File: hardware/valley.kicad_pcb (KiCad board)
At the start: 2 copper layers, 28 parts, among them IC1 ATMEGA1284P-A, P1 CONN_01X10, P2 USB_OTG, P3 CONN_02X03, P4 CONN_01X16, Q2 BSS138, U1 CH340G, U2 AP111733, U3 TXS0108E, Y1 12M

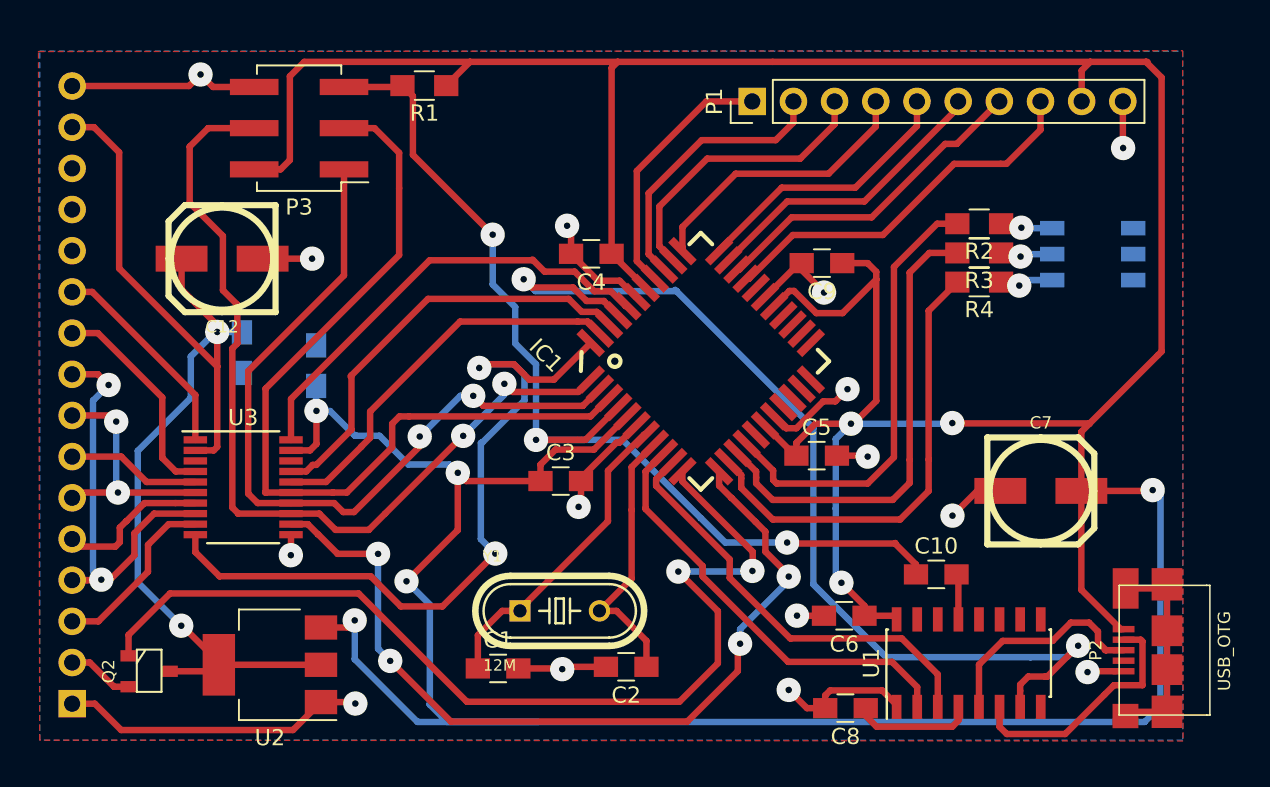
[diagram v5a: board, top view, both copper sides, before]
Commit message: ESP12E version laid out.
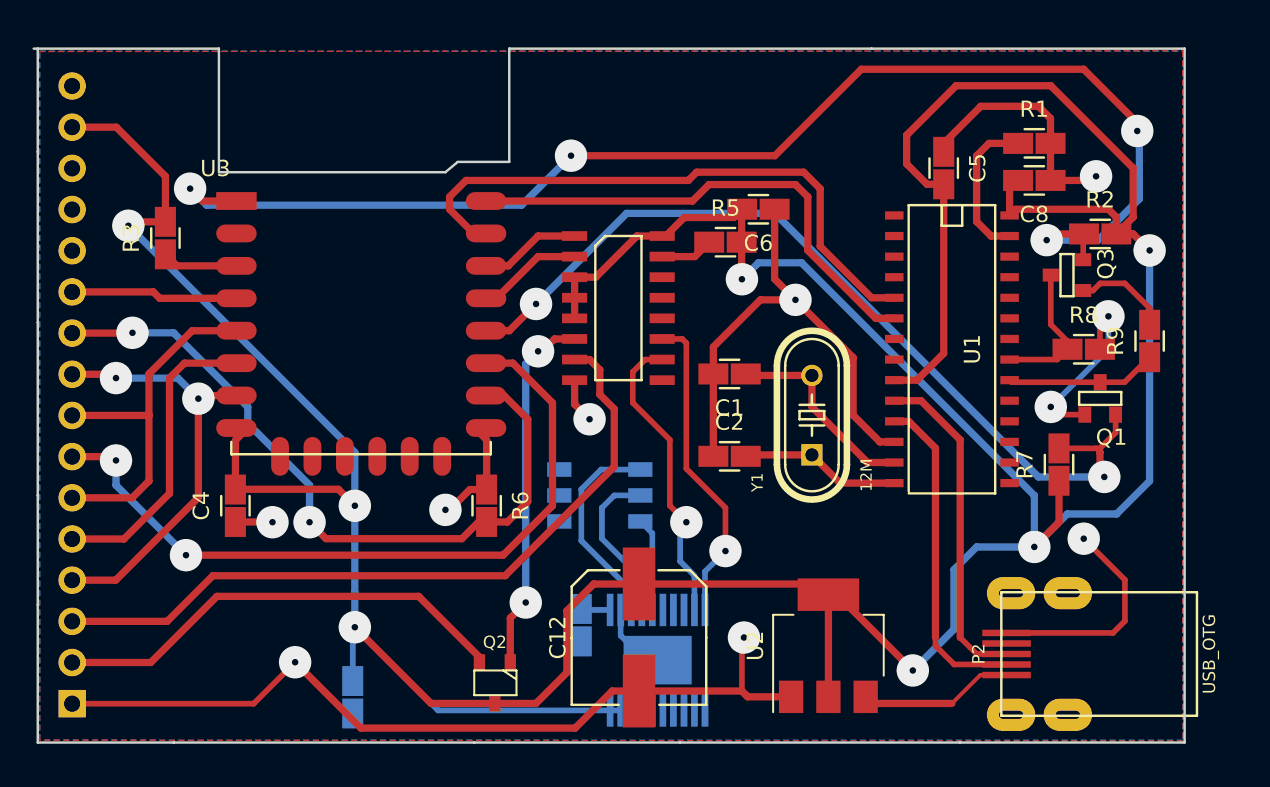
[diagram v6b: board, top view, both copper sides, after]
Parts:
- removed C10, C11, C13, C9: 0.1u, Capacitors_SMD:C_0805_HandSoldering
- removed C7: 47u, cbrues/kicad-lib2/footprints/capacitors.pretty:SMD_PANASONIC_D
- removed P1: CONN_01X10, Pin_Headers:Pin_Header_Straight_1x10_Pitch2.54mm
- removed P3: CONN_02X03, Pin_Headers:Pin_Header_Straight_2x03_Pitch2.54mm_SMD
- added ??1: PCA9557, adamgreig/agg-kicad/agg.pretty:SOIC-16, F.Cu at (155.2, 53.8)
- added Q1: PDTD113ZT,215, celeritous/KiCad.pretty:SOT23-3, F.Cu at (184.9, 58.4)
- added Q3: PDTD113ZT,215, celeritous/KiCad.pretty:SOT23-3, F.Cu at (181.9, 51.8)
- added R5: 2k, coddingtonbear/coddingtonbear.pretty:0805_Milling, F.Cu at (161.8, 49.8)
- added R6: 100k, coddingtonbear/coddingtonbear.pretty:0805_Milling, F.Cu at (147.1, 66.0)
- added R7: 4.7k, coddingtonbear/coddingtonbear.pretty:0805_Milling, F.Cu at (182.4, 63.5)
- added R8: 10k, coddingtonbear/coddingtonbear.pretty:0805_Milling, F.Cu at (183.9, 56.4)
- added R9: 10k, coddingtonbear/coddingtonbear.pretty:0805_Milling, F.Cu at (188.0, 55.9)
- C1, C2, C4, C5, C6, C8: footprint Capacitors_SMD:C_0805_HandSoldering -> coddingtonbear/coddingtonbear.pretty:0805_Milling
- C12: value 47u -> 1000u; footprint cbrues/kicad-lib2/footprints/capacitors.pretty:SMD_PANASONIC_D -> ohdsp/KiCad-Libs/MyKiCadLibs-Footprints.pretty:CAP-SMD-SIZE-F
- C3: footprint Capacitors_SMD:C_0805_HandSoldering -> coddingtonbear/coddingtonbear.pretty:0805_Milling; moved to B.Cu
- IC1: value ATMEGA1284P-A -> TLC5971_SOP; footprint OLIMEX/KiCAD/KiCAD_Footprints/OLIMEX_IC-FP.pretty:TQFP44 -> brunoeagle/kicad-open-modules:TSSOP-20; moved to B.Cu
- P2: footprint valley:MICRO-B_USB-INVERTED -> coddingtonbear/coddingtonbear.pretty:UJ2-MIBH-4-SMT
- R1: value 10k -> R; footprint Resistors_SMD:R_0805_HandSoldering -> coddingtonbear/coddingtonbear.pretty:0805_Milling
- R2, R3: value 1.5k -> 10k; footprint Resistors_SMD:R_0805_HandSoldering -> coddingtonbear/coddingtonbear.pretty:0805_Milling
- R4: value 1k -> 5k; footprint Resistors_SMD:R_0805_HandSoldering -> coddingtonbear/coddingtonbear.pretty:0805_Milling; moved to B.Cu
- U1: value CH340G -> CH341A; footprint Housings_SOIC:SOIC-16_3.9x9.9mm_Pitch1.27mm -> KiCad/SMD_Packages.pretty:SOIC-28
- U3: value TXS0108E -> ESP-12E; footprint Housings_SSOP:TSSOP-20_4.4x6.5mm_Pitch0.65mm -> coddingtonbear/coddingtonbear.pretty:ESP-12E
- moved R3 50.2 mm to (127.3, 49.5), turned to 90 degrees
- moved R1 37.8 mm to (180.8, 43.7), turned to 0 degrees
- moved C12 34.7 mm to (156.5, 74.2), turned to 0 degrees
- moved C8 34.6 mm to (180.8, 46.0)
- moved U2 34.5 mm to (168.1, 74.7), turned to 90 degrees
- moved D1 33.8 mm to (154.1, 65.4), turned to 0 degrees
- moved R4 32.4 mm to (152.9, 73.4), turned to 270 degrees
- moved C4 26.9 mm to (131.6, 66.0), turned to 90 degrees
- moved C6 25.6 mm to (163.8, 47.8)
- moved C1 23.1 mm to (162.1, 57.9), turned to 180 degrees
- moved Q2 21.3 mm to (147.6, 77.0), turned to 180 degrees
- moved Y1 19.7 mm to (167.1, 60.5), turned to 90 degrees
- moved C5 19.4 mm to (175.3, 45.2), turned to 270 degrees
- moved U1 19.4 mm to (175.8, 56.4), turned to 270 degrees
- moved IC1 18.6 mm to (157.6, 75.6), turned to 0 degrees
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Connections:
- C2 pad 1: Net-(C2-Pad1) -> GND
- C2 pad 2: GND -> Net-(C2-Pad2)
- C3 pad 1: +5V -> GND
- C3 pad 2: GND -> +3V3
- C4 pad 1: +5V -> GND
- C4 pad 2: GND -> +3V3
- C5 pad 1: +5V -> GND
- C5 pad 2: GND -> +3V3
- C6 pad 1: +5V -> GND
- C6 pad 2: GND -> +3V3
- C8 pad 1: Net-(C8-Pad1) -> GND
- C8 pad 2: GND -> +3V3
- D1 pad 4: Net-(D1-Pad4) -> LED_BLUE
- D1 pad 5: Net-(D1-Pad5) -> LED_GREEN
- D1 pad 6: Net-(D1-Pad6) -> LED_RED
- IC1 pad 1: MOSI -> Net-(IC1-Pad1)
- IC1 pad 10: TXD -> Net-(??1-Pad11)
- IC1 pad 11: BACKLIGHT -> Net-(IC1-Pad11)
- IC1 pad 12: CS_SD -> Net-(IC1-Pad12)
- IC1 pad 13: LED_RED -> Net-(IC1-Pad13)
- IC1 pad 14: LED_GREEN -> Net-(IC1-Pad14)
- IC1 pad 15: LED_BLUE -> Net-(IC1-Pad15)
- IC1 pad 17: +5V -> Net-(IC1-Pad17)
- IC1 pad 18: GND -> Net-(IC1-Pad18)
- IC1 pad 19: Net-(IC1-Pad19) -> +3V3
- IC1 pad 2: MISO -> GND
- IC1 pad 20: Net-(IC1-Pad20) -> +3V3
- IC1 pad 21: Net-(IC1-Pad21) -> GND
- IC1 pad 3: SCK -> LED_RED
- IC1 pad 4: RESET -> LED_GREEN
- IC1 pad 5: +5V -> LED_BLUE
- IC1 pad 6: GND -> Net-(IC1-Pad6)
- IC1 pad 7: Net-(C1-Pad1) -> Net-(IC1-Pad7)
- IC1 pad 8: Net-(C2-Pad1) -> Net-(IC1-Pad8)
- IC1 pad 9: RXD -> Net-(??1-Pad10)
- P2 pad 2: Net-(P2-Pad2) -> UD-
- P2 pad 3: Net-(P2-Pad3) -> UD+
- P2 pad 6: Net-(P2-Pad6) -> GND
- P4 pad 10: Net-(P4-Pad10) -> A0
- P4 pad 11: Net-(P4-Pad11) -> RESET_TFT
- P4 pad 3: Net-(P4-Pad3) -> CS_SD
- P4 pad 4: Net-(P4-Pad4) -> MOSI
- P4 pad 5: Net-(P4-Pad5) -> MISO
- P4 pad 6: Net-(P4-Pad6) -> SCK
- P4 pad 7: Net-(P4-Pad7) -> CS_TFT
- P4 pad 8: Net-(P4-Pad6) -> SCK
- P4 pad 9: Net-(P4-Pad4) -> MOSI
- R1 pad 1: +5V -> Net-(R1-Pad1)
- R1 pad 2: RESET -> GND
- R2 pad 1: Net-(D1-Pad4) -> REST
- R2 pad 2: LED_BLUE -> +3V3
- R3 pad 1: Net-(D1-Pad5) -> Net-(R3-Pad1)
- R3 pad 2: LED_GREEN -> +3V3
- R4 pad 1: Net-(D1-Pad6) -> Net-(IC1-Pad1)
- R4 pad 2: LED_RED -> GND
- U1 pad 1: GND -> Net-(U1-Pad1)
- U1 pad 10: Net-(U1-Pad10) -> UD+
- U1 pad 11: Net-(U1-Pad11) -> UD-
- U1 pad 12: Net-(U1-Pad12) -> GND
- U1 pad 13: Net-(C10-Pad2) -> Net-(C1-Pad1)
- U1 pad 14: Net-(U1-Pad14) -> Net-(C2-Pad2)
- U1 pad 16: +5V -> Net-(U1-Pad16)
- U1 pad 2: RXD -> Net-(U1-Pad2)
- U1 pad 3: TXD -> Net-(U1-Pad3)
- U1 pad 4: Net-(C8-Pad1) -> Net-(U1-Pad4)
- U1 pad 5: Net-(P2-Pad3) -> RXD
- U1 pad 6: Net-(P2-Pad2) -> TXD
- U1 pad 7: CLKO -> Net-(U1-Pad7)
- U1 pad 9: Net-(U1-Pad9) -> +3V3
- U3 pad 1: Net-(P4-Pad11) -> REST
- U3 pad 10: ENABLE_LC -> A0
- U3 pad 11: GND -> CS_TFT
- U3 pad 12: CS_SD -> GPIO0
- U3 pad 13: MOSI -> SDA
- U3 pad 14: MISO -> SCL
- U3 pad 15: SCK -> RXD
- U3 pad 16: CS_TFT -> TXD
- U3 pad 17: A0 -> Net-(U3-Pad17)
- U3 pad 19: +5V -> Net-(U3-Pad19)
- U3 pad 2: +3V3 -> Net-(U3-Pad2)
- U3 pad 20: RESET_TFT -> Net-(U3-Pad20)
- U3 pad 3: Net-(U3-Pad3) -> Net-(R3-Pad1)
- U3 pad 4: Net-(P4-Pad10) -> RESET_TFT
- U3 pad 5: Net-(P4-Pad7) -> SCK
- U3 pad 6: Net-(P4-Pad6) -> MISO
- U3 pad 7: Net-(P4-Pad5) -> MOSI
- U3 pad 8: Net-(P4-Pad4) -> +3V3
- U3 pad 9: Net-(P4-Pad3) -> GND
- Y1 pad 1: Net-(C1-Pad1) -> Net-(C2-Pad2)
- Y1 pad 2: Net-(C2-Pad1) -> Net-(C1-Pad1)
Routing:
- net +5V: track 303.6 -> 9.58 mm, vias 8 -> 0
- net +3V3: track 69.2 -> 267.9 mm, vias 2 -> 7
- net REST: track 0.00 -> 83.1 mm, vias 0 -> 4
- net CLKO: track 62.6 -> 0.00 mm, vias 2 -> 0
- net RESET: track 62.1 -> 0.00 mm, vias 3 -> 0
- net GPIO0: track 0.00 -> 55.5 mm, vias 0 -> 2
- net ENABLE_LC: track 46.3 -> 0.00 mm, vias 2 -> 0
- net GND: track 86.2 -> 129.2 mm, vias 15 -> 8
- net BACKLIGHT: track 61.7 -> 22.5 mm
- net SCK: track 52.9 -> 23.7 mm
- net MISO: track 48.6 -> 19.5 mm, vias 2 -> 0
- net MOSI: track 55.4 -> 27.5 mm
- net Net-(P4-Pad4): track 26.2 -> 0.00 mm, vias 2 -> 0
- net Net-(P4-Pad2): track 4.10 -> 28.7 mm
- net Net-(IC1-Pad30): track 23.7 -> 0.00 mm
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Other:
- board outline added: 71 x 42.8 mm
- net class Default: trace_width 0.4 -> 0.45; via_dia 1.5 -> 2
- net class Power: trace_width 0.4 -> 0.45; via_dia 1.5 -> 2

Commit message: Removing top copper nonsignal layer.
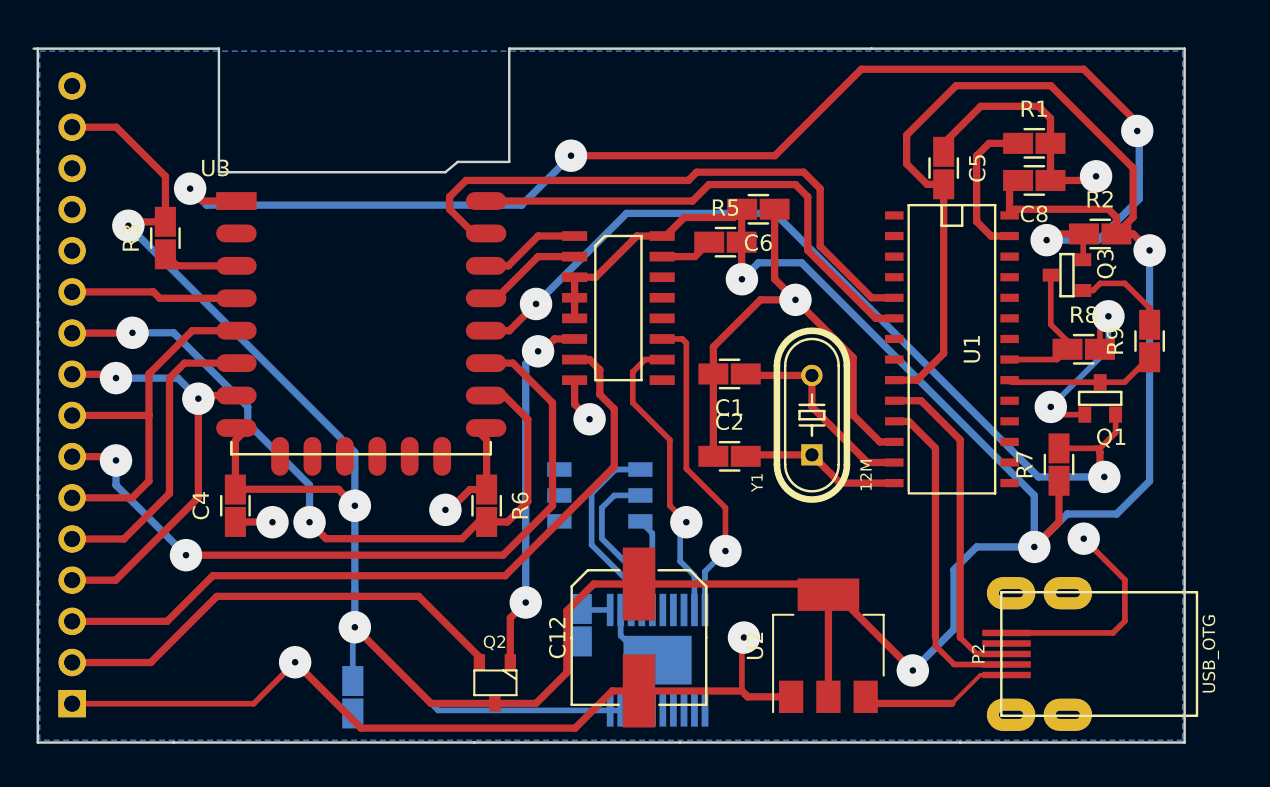
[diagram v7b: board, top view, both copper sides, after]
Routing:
- net LED_RED: track 12.9 -> 11.8 mm
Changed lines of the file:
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@@
   (segment (start 154.178 68.072) (end 154.178 66.167) (width 0.35) (layer B.Cu) (net 7))
   (segment (start 156.63672 70.53072) (end 154.178 68.072) (width 0.35) (layer B.Cu) (net 7))
-  (segment (start 155.98648 72.4662) (end 155.98648 71.27748) (width 0.35) (layer B.Cu) (net 8) (status 400000))
-  (segment (start 154.1272 63.8048) (end 156.55036 63.8048) (width 0.35) (layer B.Cu) (net 8) (status 800000))
-  (segment (start 152.908 65.024) (end 154.1272 63.8048) (width 0.35) (layer B.Cu) (net 8))
-  (segment (start 152.908 68.199) (end 152.908 65.024) (width 0.35) (layer B.Cu) (net 8))
-  (segment (start 155.98648 71.27748) (end 152.908 68.199) (width 0.35) (layer B.Cu) (net 8))
+  (segment (start 155.98648 72.4662) (end 155.98648 70.89648) (width 0.35) (layer B.Cu) (net 8) (status 400000))
+  (segment (start 155.0162 63.8048) (end 156.55036 63.8048) (width 0.35) (layer B.Cu) (net 8) (status 800000))
+  (segment (start 153.543 65.278) (end 155.0162 63.8048) (width 0.35) (layer B.Cu) (net 8))
+  (segment (start 153.543 68.453) (end 153.543 65.278) (width 0.35) (layer B.Cu) (net 8))
+  (segment (start 155.98648 70.89648) (end 153.543 68.453) (width 0.35) (layer B.Cu) (net 8))
   (segment (start 129.286 59.436) (end 129.286 65.532) (width 0.45) (layer F.Cu) (net 9))
   (segment (start 124.188 70.63) (end 121.5 70.63) (width 0.45) (layer F.Cu) (net 9) (status 800000))
@@
       )
     )
-  )
-  (zone (net 0) (net_name "") (layer F.Cu) (hatch edge 0.508)
-    (connect_pads (clearance 0.45))
-    (min_thickness 0.254)
-    (fill yes (arc_segments 16) (thermal_gap 0.808) (thermal_bridge_width 0.508))
-    (polygon
-      (pts
-        (xy 190.025 80.55) (xy 119.5 80.5) (xy 119.425044 38.025) (xy 190 37.975)
-      )
-    )

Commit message: I just realized that I don't need a ground plane -- with milling, I get a copper layer for free.
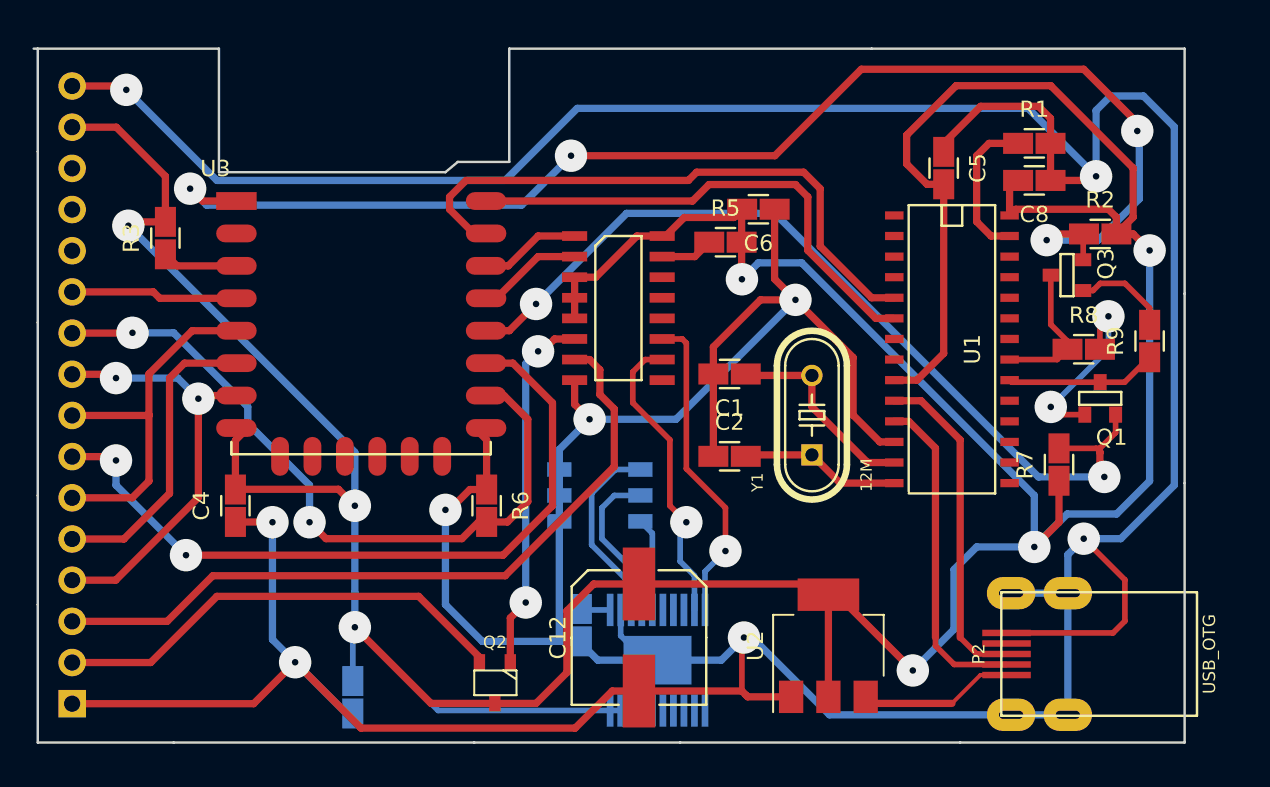
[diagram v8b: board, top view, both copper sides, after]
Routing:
- net GND: track 129.2 -> 345.9 mm, vias 8 -> 9
- removed copper zone on B.Cu, net GND
